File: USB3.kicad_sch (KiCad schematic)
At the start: 19 parts, among them U1 TUSB7340, Y1 Crystal_Small

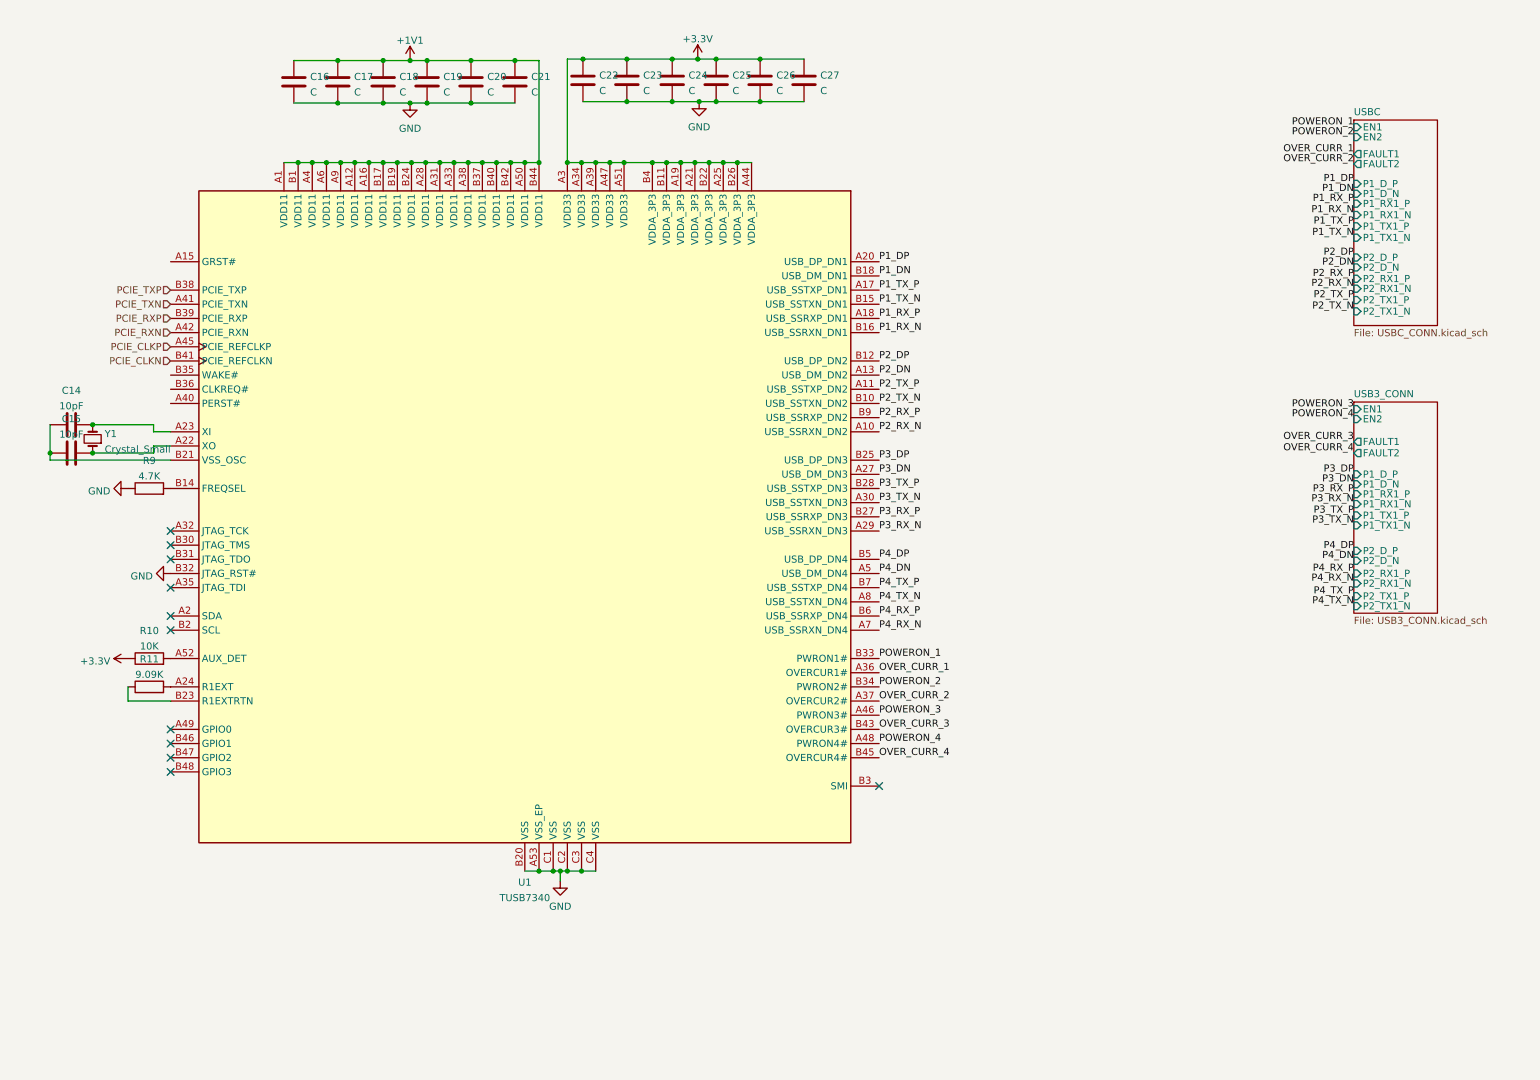
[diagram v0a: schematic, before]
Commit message: Initial layout and all parts added. Some pins still not connected to power
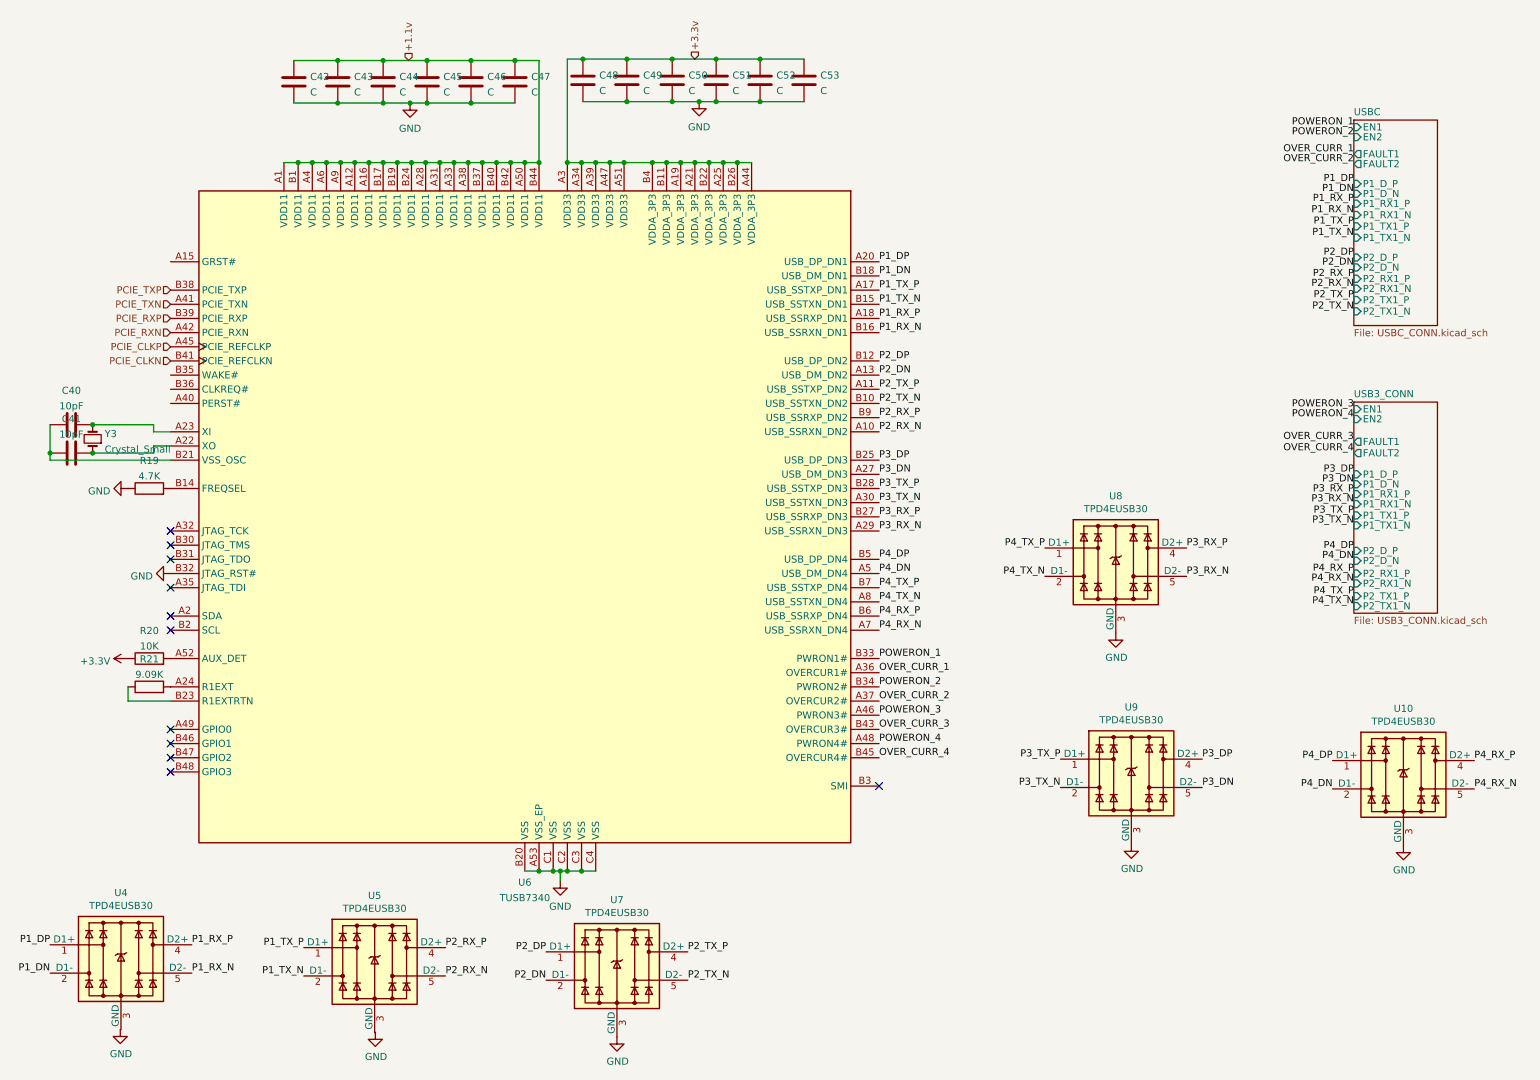
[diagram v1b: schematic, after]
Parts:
- added U10, U4, U5, U7, U8, U9: TPD4EUSB30, Package_SON:USON-10_2.5x1.0mm_P0.5mm, symbol CM4IO:TPD4EUSB30
- renumbered C14 to C40, C15 to C41, C16 to C42, C17 to C43, C18 to C44, C19 to C45, C20 to C46, C21 to C47, C22 to C48, C23 to C49, C24 to C50, C25 to C51, C26 to C52, C27 to C53, R9 to R19, R10 to R20, R11 to R21, U1 to U6, Y1 to Y3
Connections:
- net +3V3: no longer C48.1, C49.1, C50.1, C51.1, C52.1, C53.1, U6.A19 (VDDA_3P3), U6.A21 (VDDA_3P3), U6.A25 (VDDA_3P3), U6.A3 (VDD33), U6.A34 (VDD33), U6.A39 (VDD33), U6.A44 (VDDA_3P3), U6.A47 (VDD33), U6.A51 (VDD33), U6.B11 (VDDA_3P3), U6.B22 (VDDA_3P3), U6.B26 (VDDA_3P3), U6.B4 (VDDA_3P3)
- net GND: now also U10.3 (GND), U10.8 (GND), U7.3 (GND), U7.8 (GND), U8.3 (GND), U8.8 (GND), U9.3 (GND), U9.8 (GND)
- net P1_DN: now also U4.2 (D1-), U4.9
- net P1_DP: now also U4.1 (D1+), U4.10
- net P1_RX_N: now also U4.5 (D2-), U4.6
- net P1_RX_P: now also U4.4 (D2+), U4.7
- net P1_TX_N: now also U5.2 (D1-), U5.9
- net P1_TX_P: now also U5.1 (D1+), U5.10
- net P2_DN: now also U7.2 (D1-), U7.9
- net P2_DP: now also U7.1 (D1+), U7.10
- net P2_RX_N: now also U5.5 (D2-), U5.6
- net P2_RX_P: now also U5.4 (D2+), U5.7
- net P2_TX_N: now also U7.5 (D2-), U7.6
- net P2_TX_P: now also U7.4 (D2+), U7.7
- net P3_DN: now also U9.5 (D2-), U9.6
- net P3_DP: now also U9.4 (D2+), U9.7
- net P3_RX_N: now also U8.5 (D2-), U8.6
- net P3_RX_P: now also U8.4 (D2+), U8.7
- net P3_TX_N: now also U9.2 (D1-), U9.9
- net P3_TX_P: now also U9.1 (D1+), U9.10
- net P4_DN: now also U10.2 (D1-), U10.9
- net P4_DP: now also U10.1 (D1+), U10.10
- net P4_RX_N: now also U10.5 (D2-), U10.6
- net P4_RX_P: now also U10.4 (D2+), U10.7
- net P4_TX_N: now also U8.2 (D1-), U8.9
- net P4_TX_P: now also U8.1 (D1+), U8.10
- net +1V1 renamed +1.1v
- new net: U4.3 (GND), U4.8 (GND)
- new net: U5.3 (GND), U5.8 (GND)
- new net +3.3v: C48.1, C49.1, C50.1, C51.1, C52.1, C53.1, U6.A19 (VDDA_3P3), U6.A21 (VDDA_3P3), U6.A25 (VDDA_3P3), U6.A3 (VDD33), U6.A34 (VDD33), U6.A39 (VDD33), U6.A44 (VDDA_3P3), U6.A47 (VDD33), U6.A51 (VDD33), U6.B11 (VDDA_3P3), U6.B22 (VDDA_3P3), U6.B26 (VDDA_3P3), U6.B4 (VDDA_3P3)

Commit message: Diff pairs routed
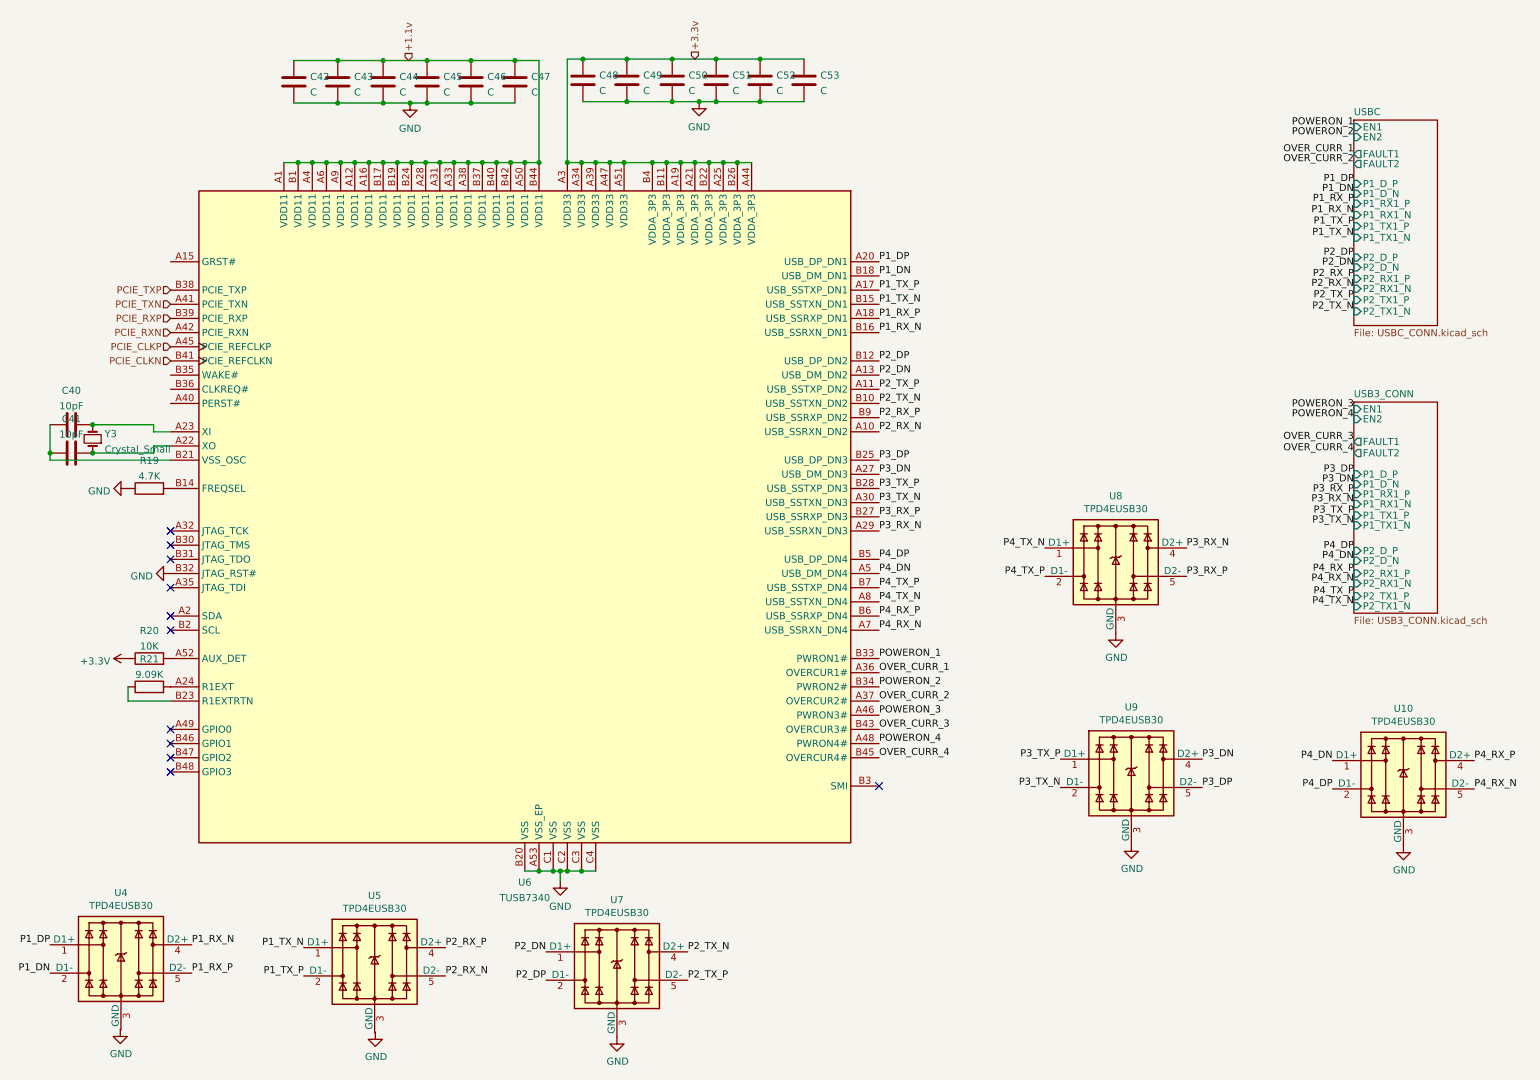
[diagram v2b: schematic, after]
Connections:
- net P1_RX_N: now also U4.4 (D2+), U4.7; no longer U4.5 (D2-), U4.6
- net P1_RX_P: now also U4.5 (D2-), U4.6; no longer U4.4 (D2+), U4.7
- net P1_TX_N: now also U5.1 (D1+), U5.10; no longer U5.2 (D1-), U5.9
- net P1_TX_P: now also U5.2 (D1-), U5.9; no longer U5.1 (D1+), U5.10
- net P2_DN: now also U7.1 (D1+), U7.10; no longer U7.2 (D1-), U7.9
- net P2_DP: now also U7.2 (D1-), U7.9; no longer U7.1 (D1+), U7.10
- net P2_TX_N: now also U7.4 (D2+), U7.7; no longer U7.5 (D2-), U7.6
- net P2_TX_P: now also U7.5 (D2-), U7.6; no longer U7.4 (D2+), U7.7
- net P3_DN: now also U9.4 (D2+), U9.7; no longer U9.5 (D2-), U9.6
- net P3_DP: now also U9.5 (D2-), U9.6; no longer U9.4 (D2+), U9.7
- net P3_RX_N: now also U8.4 (D2+), U8.7; no longer U8.5 (D2-), U8.6
- net P3_RX_P: now also U8.5 (D2-), U8.6; no longer U8.4 (D2+), U8.7
- net P4_DN: now also U10.1 (D1+), U10.10; no longer U10.2 (D1-), U10.9
- net P4_DP: now also U10.2 (D1-), U10.9; no longer U10.1 (D1+), U10.10
- net P4_TX_N: now also U8.1 (D1+), U8.10; no longer U8.2 (D1-), U8.9
- net P4_TX_P: now also U8.2 (D1-), U8.9; no longer U8.1 (D1+), U8.10

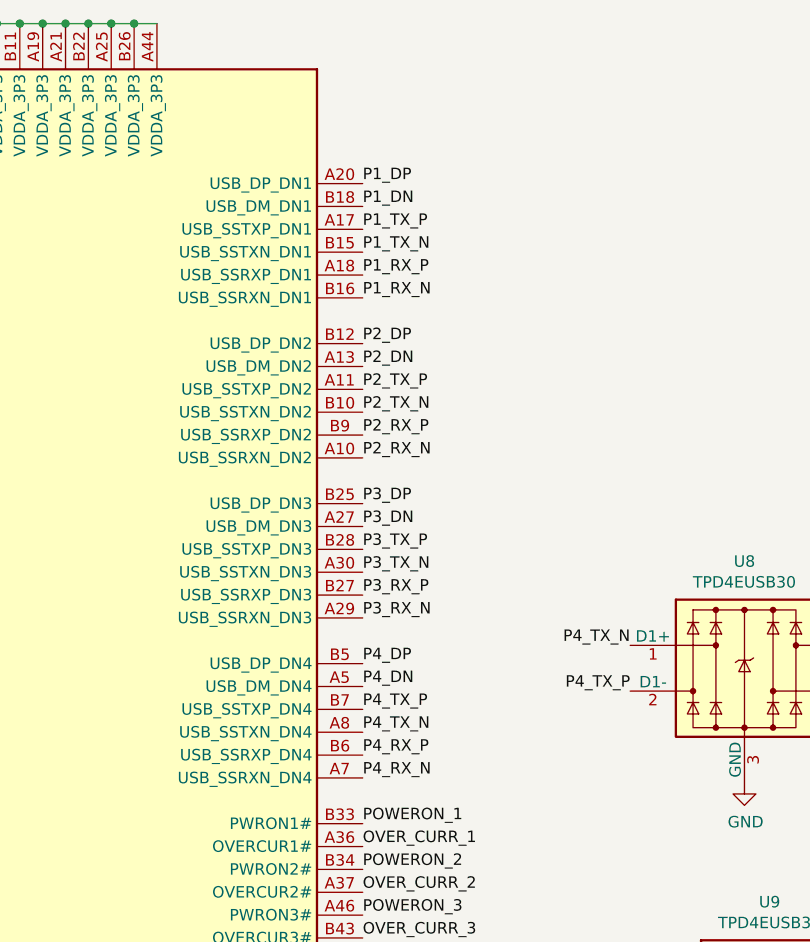
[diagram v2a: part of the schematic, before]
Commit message: mostly routed, need to add more layers fo power and finish low speed signal routing
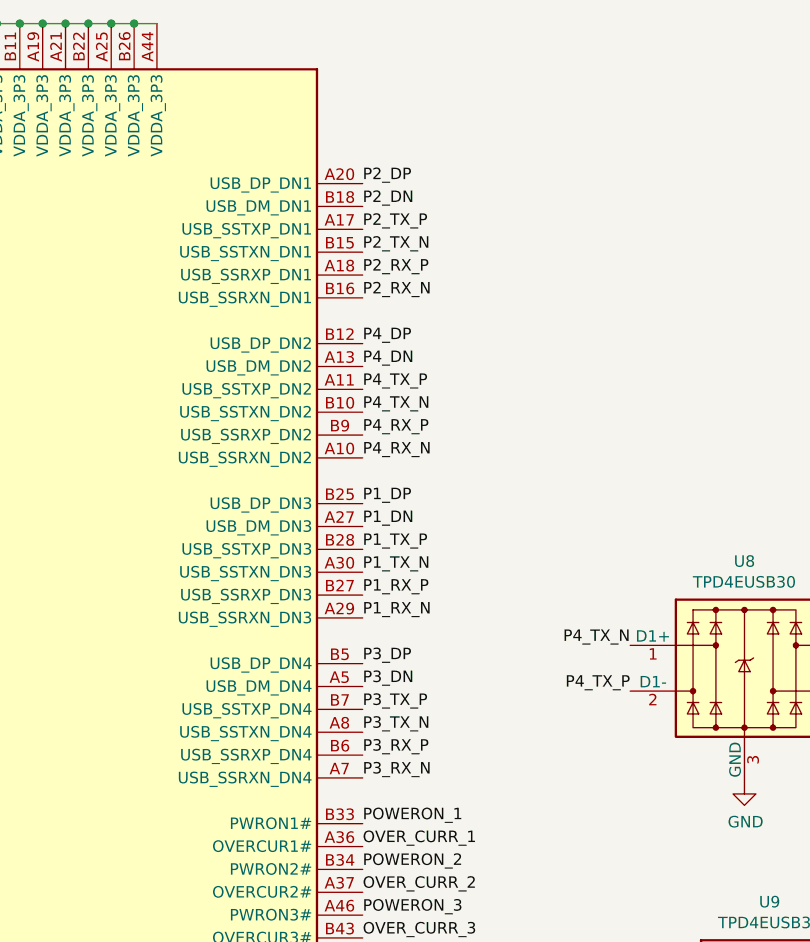
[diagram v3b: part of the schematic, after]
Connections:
- net P1_DN: now also U6.A27 (USB_DM_DN3); no longer U6.B18 (USB_DM_DN1)
- net P1_DP: now also U6.B25 (USB_DP_DN3); no longer U6.A20 (USB_DP_DN1)
- net P1_RX_N: now also U6.A29 (USB_SSRXN_DN3); no longer U6.B16 (USB_SSRXN_DN1)
- net P1_RX_P: now also U6.B27 (USB_SSRXP_DN3); no longer U6.A18 (USB_SSRXP_DN1)
- net P1_TX_N: now also U6.A30 (USB_SSTXN_DN3); no longer U6.B15 (USB_SSTXN_DN1)
- net P1_TX_P: now also U6.B28 (USB_SSTXP_DN3); no longer U6.A17 (USB_SSTXP_DN1)
- net P2_DN: now also U6.B18 (USB_DM_DN1); no longer U6.A13 (USB_DM_DN2)
- net P2_DP: now also U6.A20 (USB_DP_DN1); no longer U6.B12 (USB_DP_DN2)
- net P2_RX_N: now also U6.B16 (USB_SSRXN_DN1); no longer U6.A10 (USB_SSRXN_DN2)
- net P2_RX_P: now also U6.A18 (USB_SSRXP_DN1); no longer U6.B9 (USB_SSRXP_DN2)
- net P2_TX_N: now also U6.B15 (USB_SSTXN_DN1); no longer U6.B10 (USB_SSTXN_DN2)
- net P2_TX_P: now also U6.A17 (USB_SSTXP_DN1); no longer U6.A11 (USB_SSTXP_DN2)
- net P3_DN: now also U6.A5 (USB_DM_DN4); no longer U6.A27 (USB_DM_DN3)
- net P3_DP: now also U6.B5 (USB_DP_DN4); no longer U6.B25 (USB_DP_DN3)
- net P3_RX_N: now also U6.A7 (USB_SSRXN_DN4); no longer U6.A29 (USB_SSRXN_DN3)
- net P3_RX_P: now also U6.B6 (USB_SSRXP_DN4); no longer U6.B27 (USB_SSRXP_DN3)
- net P3_TX_N: now also U6.A8 (USB_SSTXN_DN4); no longer U6.A30 (USB_SSTXN_DN3)
- net P3_TX_P: now also U6.B7 (USB_SSTXP_DN4); no longer U6.B28 (USB_SSTXP_DN3)
- net P4_DN: now also U6.A13 (USB_DM_DN2); no longer U6.A5 (USB_DM_DN4)
- net P4_DP: now also U6.B12 (USB_DP_DN2); no longer U6.B5 (USB_DP_DN4)
- net P4_RX_N: now also U6.A10 (USB_SSRXN_DN2); no longer U6.A7 (USB_SSRXN_DN4)
- net P4_RX_P: now also U6.B9 (USB_SSRXP_DN2); no longer U6.B6 (USB_SSRXP_DN4)
- net P4_TX_N: now also U6.B10 (USB_SSTXN_DN2); no longer U6.A8 (USB_SSTXN_DN4)
- net P4_TX_P: now also U6.A11 (USB_SSTXP_DN2); no longer U6.B7 (USB_SSTXP_DN4)
